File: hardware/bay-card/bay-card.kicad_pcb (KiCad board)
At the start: 4 copper layers, 40 x 37.6 mm, 39 parts, among them J1 bay card edge, J2 SATA 22-pin, Q1 P-FET -30V 6A DFN3x3, Q2 P-FET -30V 6A DFN3x3, Q3 2N7002, Q4 2N7002, U1 ASM1153E, Y1 30MHz CL=16pF

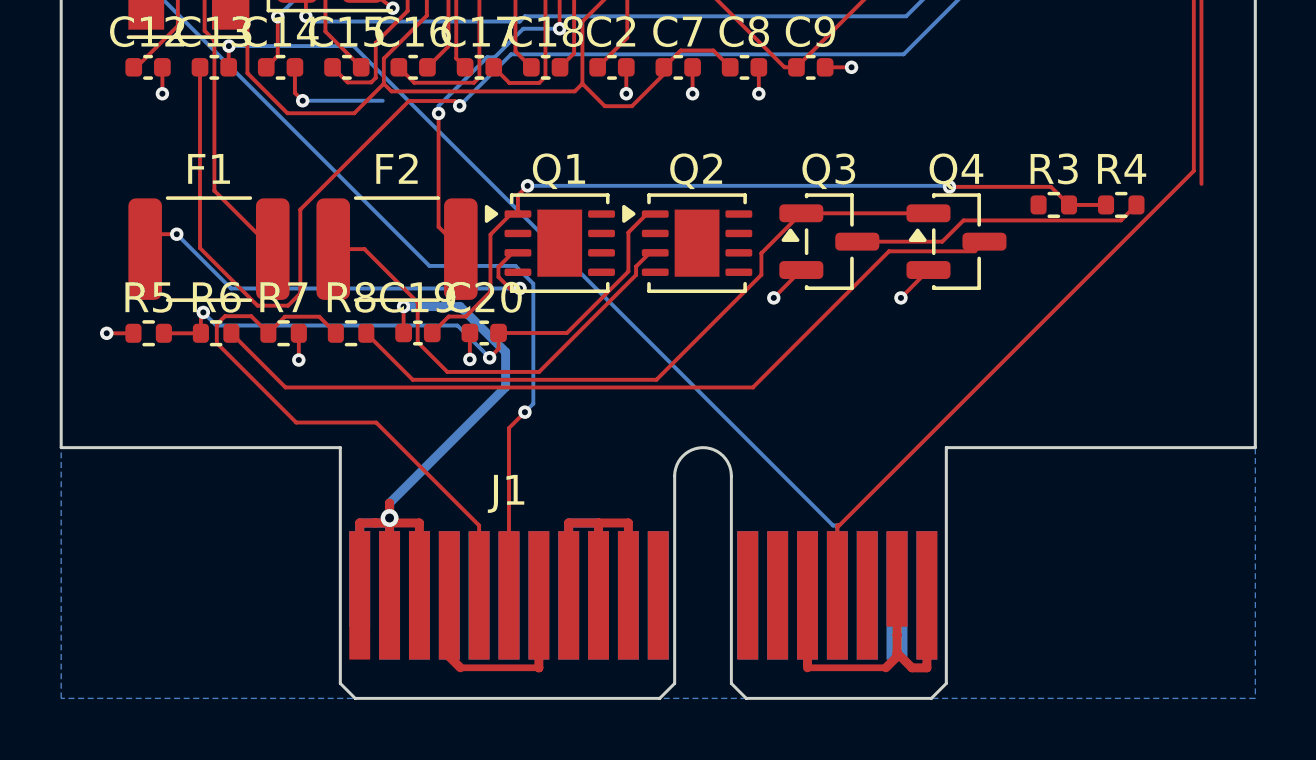
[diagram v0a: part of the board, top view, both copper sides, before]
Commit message: hw(routing): card-edge finger fanout (in-line vias shared by the A/B fingers, edge-aware collision check), DFN pins in fanout_qfn with rip-up of simple blocking nets, project-aware render script; card fanouts applied
Co-Authored-By: Claude Fable 5.1 <noreply@anthropic.com>
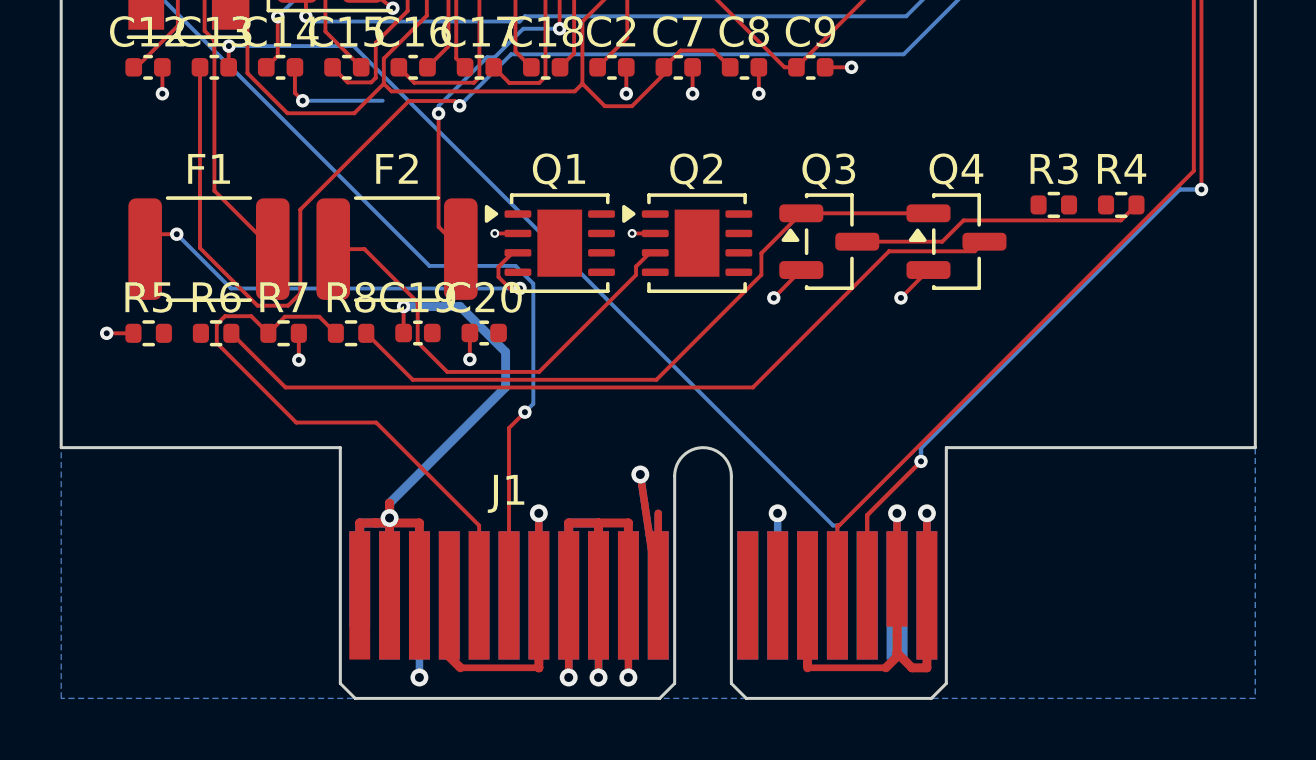
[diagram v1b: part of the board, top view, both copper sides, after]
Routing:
- net GND: track 54.7 -> 89.8 mm, vias 37 -> 43
- net Q1_G: track 26.4 -> 0.00 mm, vias 2 -> 0
- net Q2_G: track 20.8 -> 0.00 mm, vias 2 -> 0
- net USB3_RX_P: track 20.4 -> 39.2 mm, vias 0 -> 2
- net 5V_HDD: track 21.0 -> 35.5 mm, vias 6 -> 10
- net +12V: track 28.5 -> 29.3 mm, vias 2 -> 3

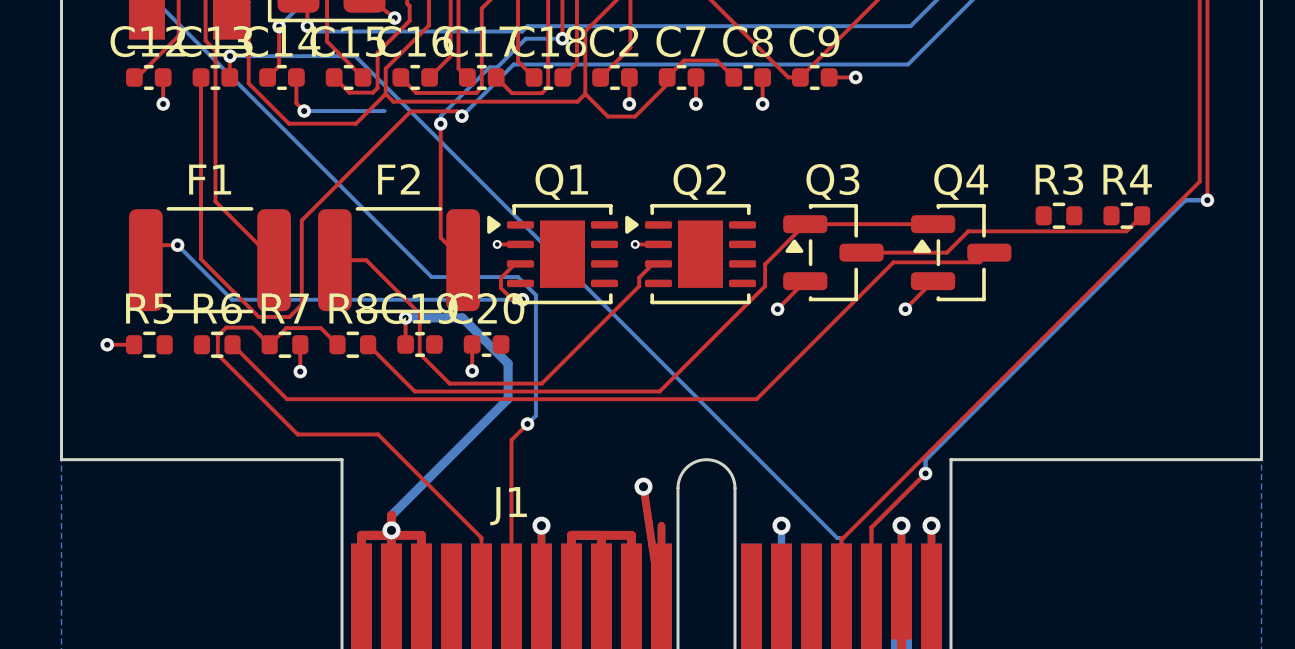
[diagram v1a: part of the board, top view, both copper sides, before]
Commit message: hw: 8-pin P-FET symbols (S 1-3, G 4, D 5-8 + EP) for Q20 / Q1 / Q2 — the generic 3-pin symbol had put G/S/D on three source pads; route.py update-nets re-syncs pad nets on a routed board; gen_sch keeps the board design rules; rules restored in both projects
Co-Authored-By: Claude Fable 5.1 <noreply@anthropic.com>
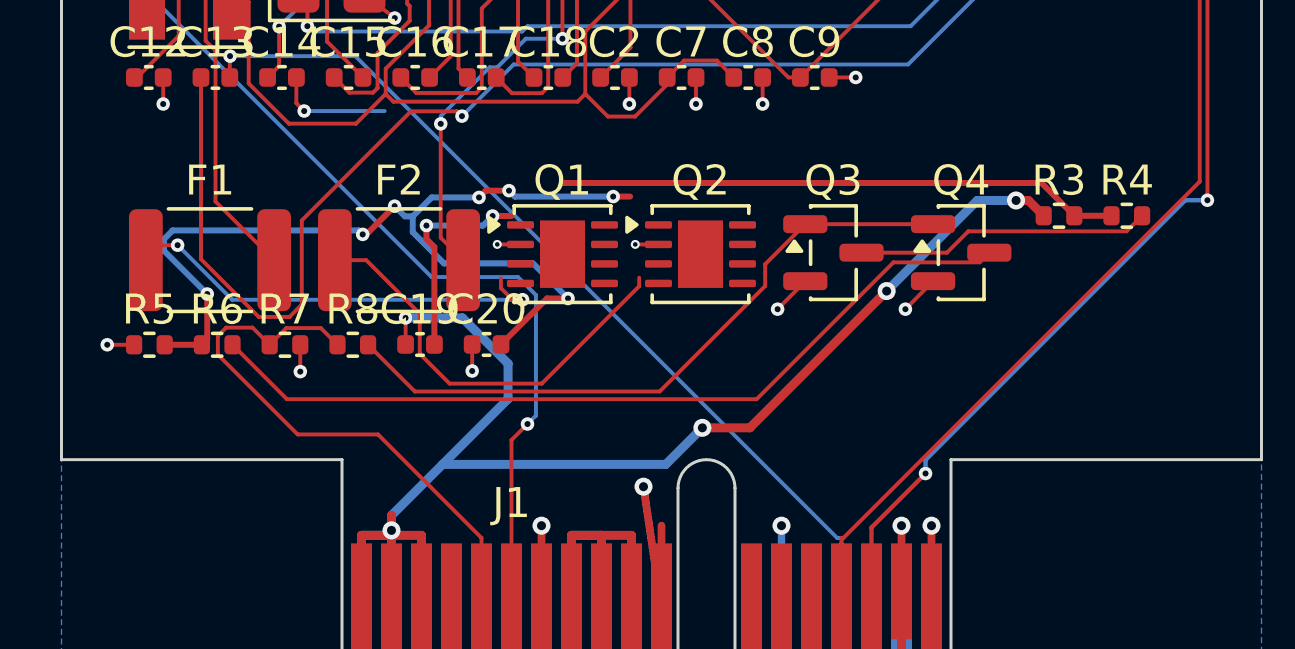
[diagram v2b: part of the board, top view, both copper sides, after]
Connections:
- Q1 pad 1: Q1_G -> +12V
- Q1 pad 3: 12V_BAY_SW -> +12V
- Q1 pad 4: (no net) -> Q1_G
- Q1 pad 5: (no net) -> 12V_BAY_SW
- Q1 pad 6: (no net) -> 12V_BAY_SW
- Q1 pad 7: (no net) -> 12V_BAY_SW
- Q1 pad 8: (no net) -> 12V_BAY_SW
- Q1 pad 9: (no net) -> 12V_BAY_SW
- Q2 pad 1: Q2_G -> 5V_HDD
- Q2 pad 3: 5V_BAY_SW -> 5V_HDD
- Q2 pad 4: (no net) -> Q2_G
- Q2 pad 5: (no net) -> 5V_BAY_SW
- Q2 pad 6: (no net) -> 5V_BAY_SW
- Q2 pad 7: (no net) -> 5V_BAY_SW
- Q2 pad 8: (no net) -> 5V_BAY_SW
- Q2 pad 9: (no net) -> 5V_BAY_SW
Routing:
- net Q2_G: track 0.00 -> 31.6 mm, vias 0 -> 7
- net Q1_G: track 0.00 -> 25.8 mm, vias 0 -> 2
- net +12V: track 29.3 -> 53.2 mm, vias 3 -> 6
- net 12V_BAY_SW: track 15.6 -> 14.7 mm
- net 5V_BAY_SW: track 15.1 -> 14.3 mm

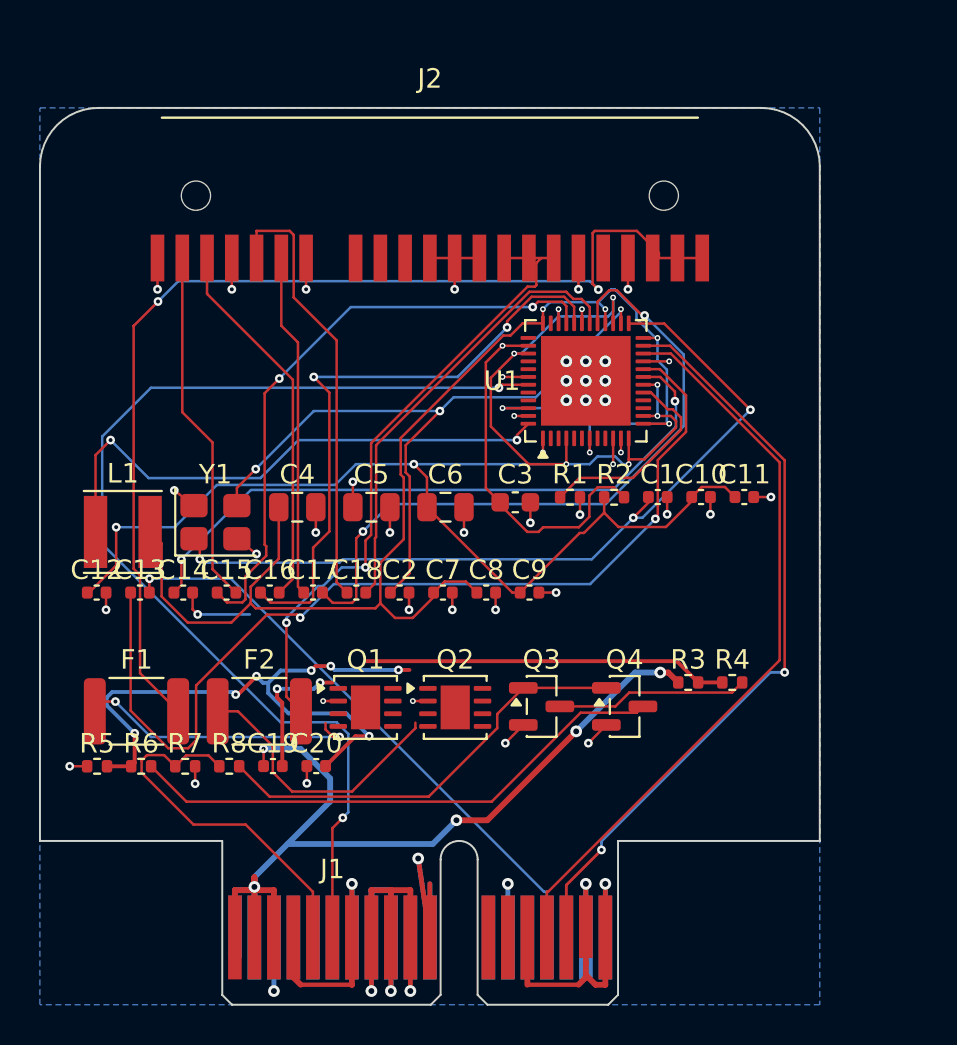
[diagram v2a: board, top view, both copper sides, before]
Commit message: hw(card): routed to 6 open connections, DRC 0 errors — pre-routing fanout with rip-up in the chain, fanout-qfn-rip command, STATUS, P-FET docs
Co-Authored-By: Claude Sonnet 5 <noreply@anthropic.com>
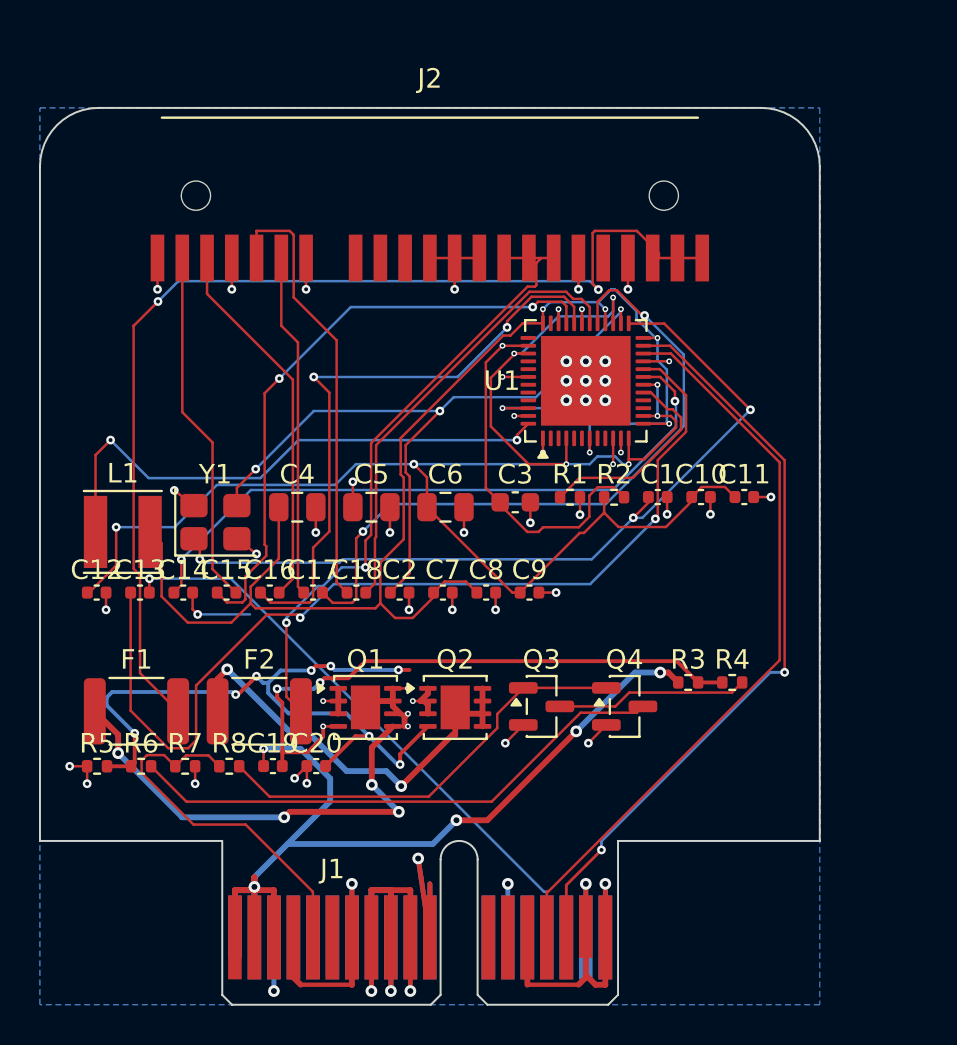
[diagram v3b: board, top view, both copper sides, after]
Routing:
- net LED_K: track 55.9 -> 0.00 mm, vias 2 -> 0
- net 12V_BAY_SW: track 14.7 -> 30.0 mm, vias 2 -> 7
- net 5V_BAY_SW: track 14.3 -> 22.5 mm, vias 0 -> 2
- net Q1_G: track 25.8 -> 31.7 mm, vias 2 -> 3
- net Q2_G: track 31.6 -> 36.3 mm, vias 7 -> 8
- net 5V_HDD: track 35.5 -> 39.0 mm, vias 10 -> 12
- net +12V: track 53.2 -> 54.5 mm

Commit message: hw(routing): pair length tuner (route.py tune) — meanders on the shorter side, layer-aware checks; card 5/8 and brain 34/44 pairs matched, DRC unchanged; in the chain
Co-Authored-By: Claude Sonnet 5 <noreply@anthropic.com>
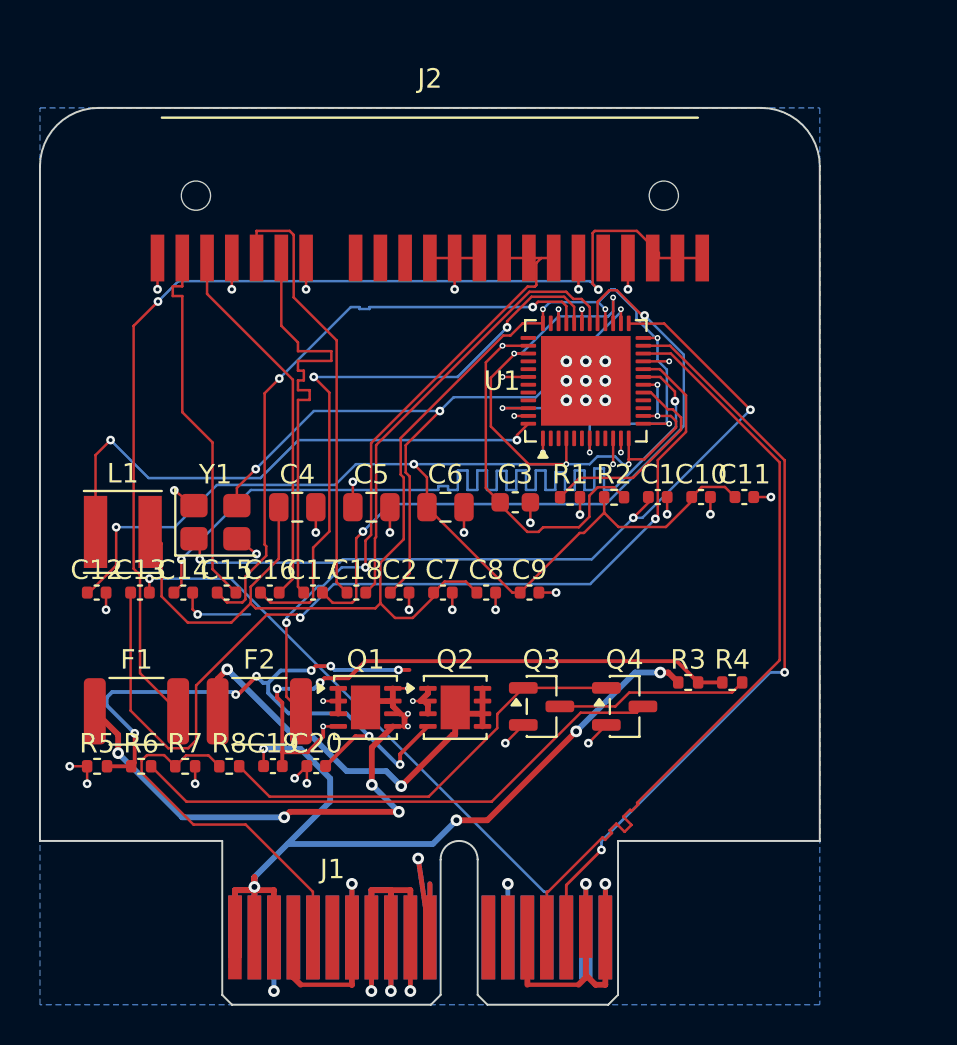
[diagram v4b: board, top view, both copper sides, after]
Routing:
- net U1_UTXN: track 33.8 -> 50.2 mm
- net SATA_B_P: track 17.6 -> 22.9 mm
- net USB3_RX_N: track 38.7 -> 40.4 mm
- net SATA_A_P: track 18.3 -> 19.3 mm

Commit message: hw(card): pairs rerouted by rip + stage 3, tuner; reroute_pairs.sh; 7 open, 6 of 8 pairs routed and matched
Co-Authored-By: Claude Sonnet 5 <noreply@anthropic.com>
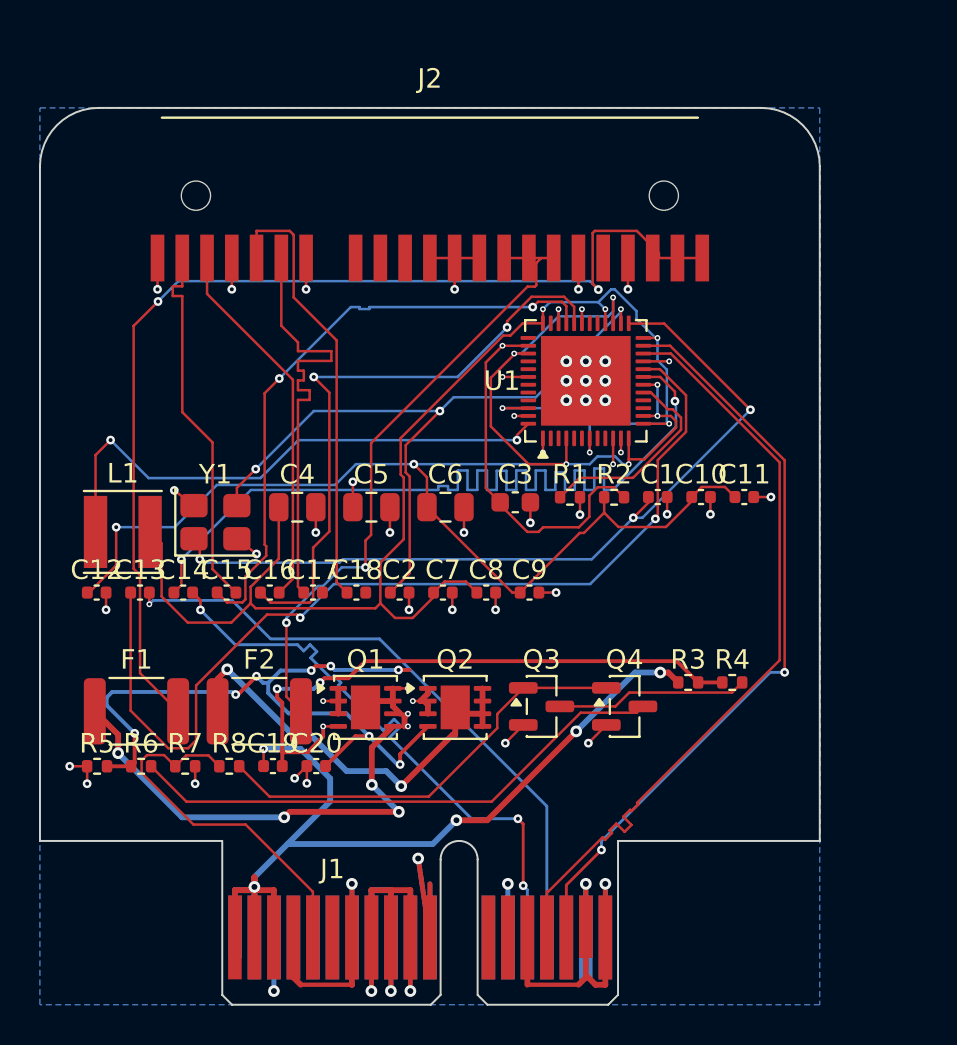
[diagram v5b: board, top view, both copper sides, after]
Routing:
- net U1_SRXP: track 35.1 -> 0.00 mm, vias 2 -> 0
- net USB3_TX_N: track 3.91 -> 31.0 mm, vias 1 -> 3
- net U1_SRXN: track 23.2 -> 0.00 mm
- net USB3_TX_P: track 30.1 -> 32.2 mm

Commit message: hw(card): pairs-first routing (stage0) — all 8 pairs routed and matched, 3 open; route_full.sh, BD_PAIRS_FIRST
Co-Authored-By: Claude Sonnet 5 <noreply@anthropic.com>
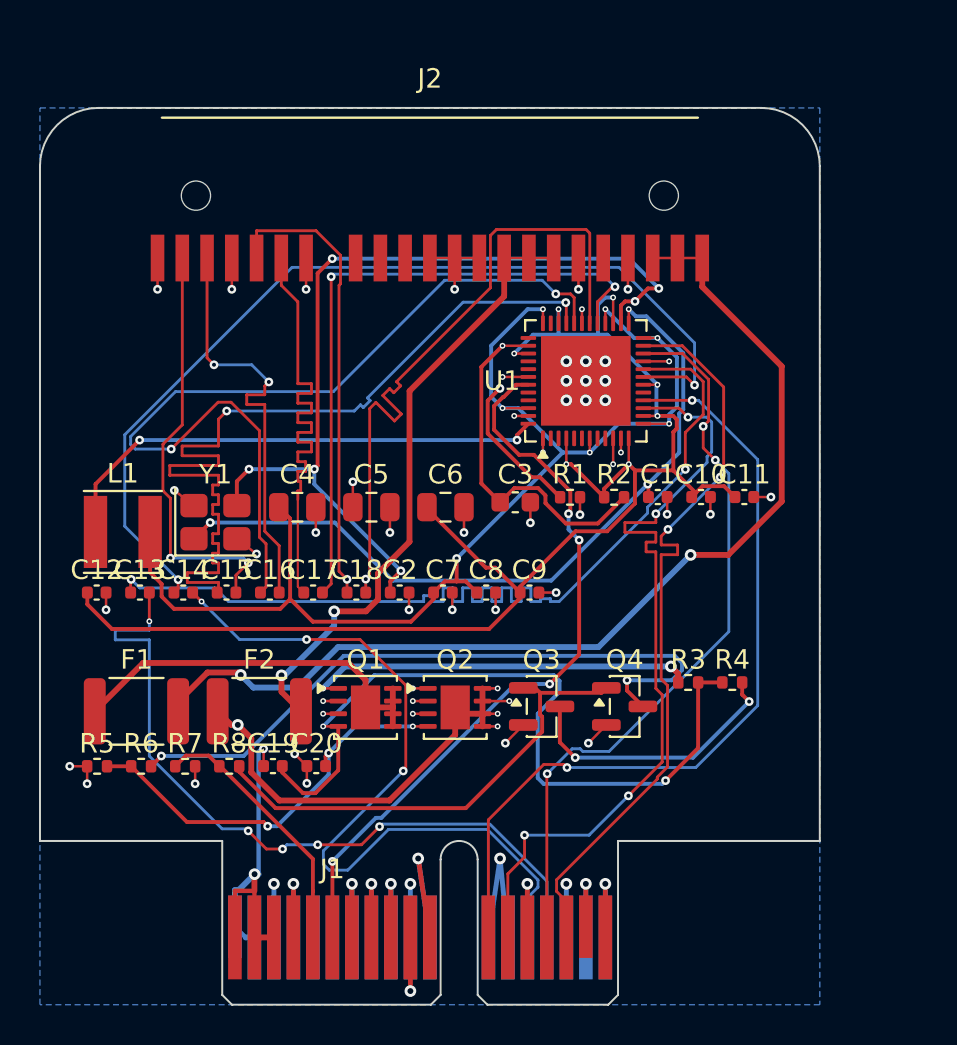
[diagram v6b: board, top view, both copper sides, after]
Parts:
- Q1, Q2: value P-FET -30V 6A DFN3x3 -> AON7403
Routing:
- net USB2_DM: track 0.00 -> 42.1 mm, vias 0 -> 2
- net USB2_DP: track 0.00 -> 40.9 mm, vias 0 -> 4
- net LED_K: track 0.00 -> 38.2 mm, vias 0 -> 4
- net U1_SRXN: track 0.00 -> 34.2 mm, vias 0 -> 1
- net U1_SRXP: track 0.00 -> 33.6 mm, vias 0 -> 2
- net 5V_HDD: track 39.0 -> 23.7 mm, vias 12 -> 14
- net Q2_G: track 36.3 -> 21.2 mm, vias 8 -> 3
- net U1_STXN: track 31.4 -> 45.0 mm
- net U1_STXP: track 31.4 -> 45.0 mm
- net +12V: track 54.5 -> 41.4 mm
- net 12V_BAY_SW: track 30.0 -> 20.0 mm, vias 7 -> 0
- net U1_XO: track 36.0 -> 45.7 mm, vias 3 -> 6
- net USB3_TX_N: track 31.0 -> 40.1 mm
- net U1_VDD_CORE: track 75.3 -> 66.6 mm, vias 6 -> 7
- net U1_VCCO: track 85.0 -> 77.0 mm, vias 9 -> 7
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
